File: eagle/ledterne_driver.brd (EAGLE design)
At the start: 24.3 x 23.1 mm, 10 parts, among them IC1 MEGA8-AI

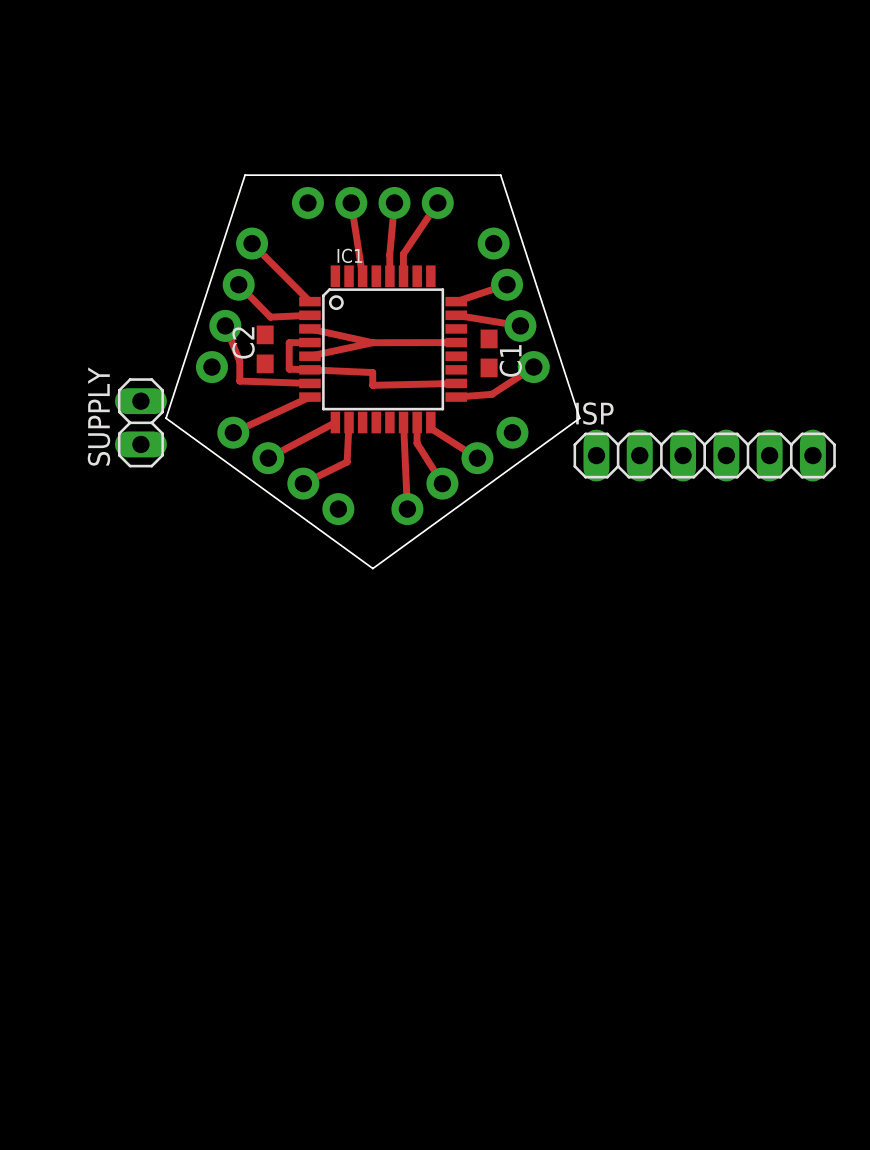
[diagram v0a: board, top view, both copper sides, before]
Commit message: Alternative routing for driver board
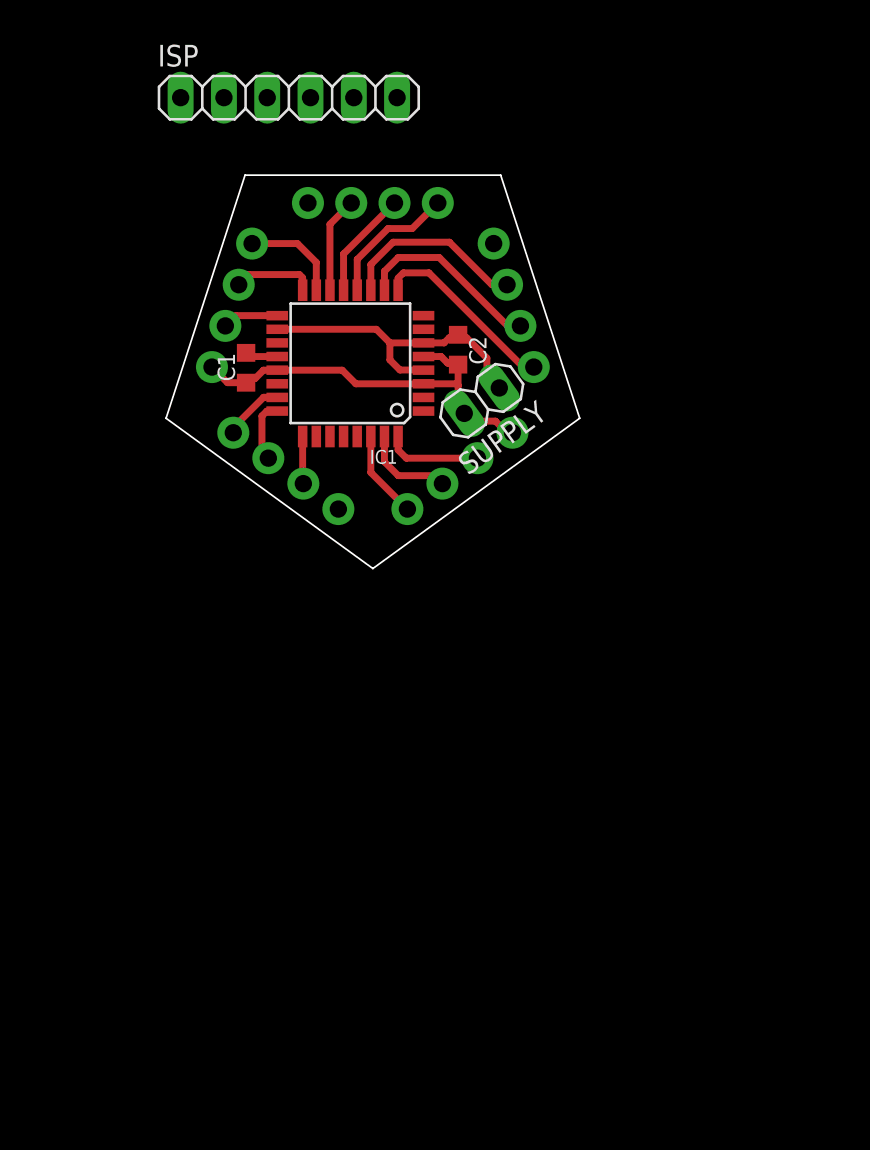
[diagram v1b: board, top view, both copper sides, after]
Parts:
- C1, C2: device rcl:C0603 -> rcl:C0603K
- moved ISP 32.2 mm to (11.6, 31.4)
- moved SUPPLY 20.0 mm to (22.9, 13.6), turned to 216 degrees
- moved C1 14.3 mm to (9.07, 15.5), turned to 90 degrees
- moved C2 11.3 mm to (21.5, 16.6), turned to 270 degrees
- moved IC1 2.09 mm to (15.2, 15.8), turned to 180 degrees
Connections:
- removed net N$2: IC1.30, JP1.3
- new net N$14: IC1.8
- new net N$15: IC1.25, JP4.3
- net MISO: now also JP5.2; no longer JP3.3
- net MOSI: now also JP5.1; no longer JP3.2
- net N$10: now also IC1.31, JP3.2; no longer IC1.10, JP4.3
- net N$11: now also IC1.32, JP3.3; no longer IC1.7, JP5.3
- net N$12: now also IC1.23; no longer IC1.8
- net N$13: now also IC1.24, JP4.2; no longer IC1.1, JP5.1
- net N$3: now also IC1.14, JP1.3; no longer IC1.28, JP1.2
- net N$4: now also IC1.13, JP1.2; no longer IC1.27, JP1.1
- net N$5: now also IC1.12, JP1.1; no longer IC1.23, JP2.2
- net N$6: now also IC1.11, JP2.3; no longer IC1.2, JP5.2
- net N$7: now also IC1.10, JP2.2; no longer IC1.24, JP2.3
- net N$8: now also IC1.9, JP2.1; no longer IC1.14, JP3.1
- net N$9: now also IC1.30, JP3.1; no longer IC1.9, JP4.2
- net SCK: now also JP5.3; no longer JP2.1
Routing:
- net GND: track 12.4 -> 24.0 mm
- net N$7: track 3.14 -> 11.1 mm
- net N$6: track 4.98 -> 11.1 mm
- net N$8: track 5.08 -> 11.1 mm
- net VCC: track 13.3 -> 18.8 mm
- net N$2: track 4.35 -> 0.00 mm
- net N$5: track 3.82 -> 7.91 mm
- net N$15: track 0.00 -> 2.78 mm
- net N$1: track 0.00 -> 1.89 mm
- net N$11: track 7.52 -> 5.64 mm
- net MOSI: track 4.01 -> 5.85 mm
- net SCK: track 5.03 -> 3.29 mm
- net N$4: track 4.91 -> 6.36 mm
- net N$12: track 4.96 -> 3.62 mm
- net N$3: track 4.31 -> 5.64 mm
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
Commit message: Replace ISP connector with solder pads
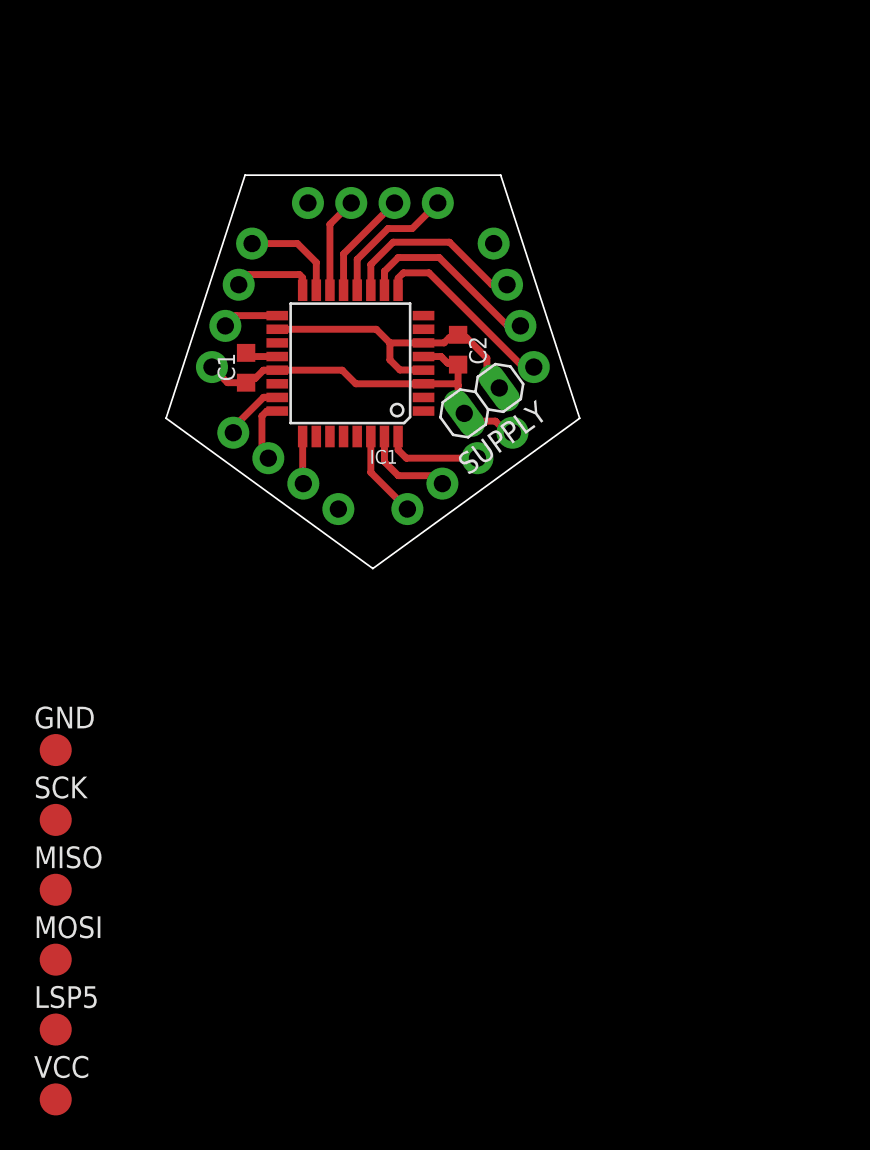
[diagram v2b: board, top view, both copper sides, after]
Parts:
- removed ISP: (no value), pinhead:1X06
- added GND, LSP5, MISO, MOSI, SCK, VCC: SOLPAD-SMD-NORMAL, solpad-smd:SOLPAD-SMD
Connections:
- net GND: now also GND.MP; no longer ISP.1
- net MISO: now also MISO.MP; no longer ISP.3
- net MOSI: now also MOSI.MP; no longer ISP.4
- net RESET: now also LSP5.MP; no longer ISP.5
- net SCK: now also SCK.MP; no longer ISP.2
- net VCC: now also VCC.MP; no longer ISP.6
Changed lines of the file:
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@@
 <attribute name="MPN" value="ATMEGA8-16AU" x="15.19" y="15.79" size="1.778" layer="27" rot="R180" display="off"/>
 </element>
-<element name="ISP" library="pinhead" package="1X06" value="" x="11.58" y="31.38"/>
 <element name="C1" library="rcl" package="C0603K" value="" x="9.07" y="15.53" rot="R90"/>
 <element name="C2" library="rcl" package="C0603K" value="" x="21.51" y="16.59" rot="R270"/>
@@
 <element name="JP5" library="pinhead_round_pads" package="1X04/90" value="" x="4.62179375" y="20.3727125" rot="MR288"/>
 <element name="SUPPLY" library="pinhead" package="1X02" value="" x="22.9" y="13.6" rot="R216"/>
+<element name="GND" library="solpad-smd" package="SOLPAD-SMD" value="SOLPAD-SMD-NORMAL" x="-2.1" y="-6.9"/>
+<element name="SCK" library="solpad-smd" package="SOLPAD-SMD" value="SOLPAD-SMD-NORMAL" x="-2.1" y="-11"/>
+<element name="MISO" library="solpad-smd" package="SOLPAD-SMD" value="SOLPAD-SMD-NORMAL" x="-2.1" y="-15.1"/>
+<element name="MOSI" library="solpad-smd" package="SOLPAD-SMD" value="SOLPAD-SMD-NORMAL" x="-2.1" y="-19.2"/>
+<element name="LSP5" library="solpad-smd" package="SOLPAD-SMD" value="SOLPAD-SMD-NORMAL" x="-2.1" y="-23.3"/>
+<element name="VCC" library="solpad-smd" package="SOLPAD-SMD" value="SOLPAD-SMD-NORMAL" x="-2.1" y="-27.4"/>
 </elements>
 <signals>
 <signal name="GND">
-<contactref element="ISP" pad="1"/>
 <contactref element="IC1" pad="21"/>
 <contactref element="IC1" pad="3"/>
@@
 <wire x1="23.7" y1="12.4" x2="24.380896875" y2="11.719103125" width="0.4064" layer="1"/>
 <wire x1="24.380896875" y1="11.719103125" x2="24.700209375" y2="11.719103125" width="0.4064" layer="1"/>
-<wire x1="20.51" y1="16.19" x2="23.597328125" y2="22.81888125" width="0" layer="19" extent="1-1"/>
-<wire x1="14.484503125" y1="7.240178125" x2="15.51" y2="14.59" width="0" layer="19" extent="1-1"/>
-<wire x1="12.7" y1="25.2" x2="10.8974" y2="15.39" width="0" layer="19" extent="1-1"/>
-<wire x1="5.23" y1="31.38" x2="12.7" y2="25.2" width="0" layer="19" extent="1-1"/>
 <wire x1="10.8974" y1="15.39" x2="10.09" y2="15.39" width="0.4064" layer="1"/>
 <wire x1="10.09" y1="15.39" x2="9.6" y2="14.9" width="0.4064" layer="1"/>
 <wire x1="9.6" y1="14.9" x2="9.315" y2="14.9" width="0.4064" layer="1"/>
 <wire x1="9.315" y1="14.9" x2="9.07" y2="14.655" width="0.4064" layer="1"/>
+<contactref element="GND" pad="MP"/>
+<wire x1="20.51" y1="16.19" x2="23.597328125" y2="22.81888125" width="0" layer="19" extent="1-1"/>
+<wire x1="14.484503125" y1="7.240178125" x2="15.51" y2="14.59" width="0" layer="19" extent="1-1"/>
+<wire x1="12.7" y1="25.2" x2="10.8974" y2="15.39" width="0" layer="19" extent="1-1"/>
+<wire x1="-2.1" y1="-6.9" x2="14.484503125" y2="7.240178125" width="0" layer="19" extent="1-1"/>
 </signal>
 <signal name="VCC">
-<contactref element="ISP" pad="6"/>
 <contactref element="IC1" pad="4"/>
 <contactref element="IC1" pad="6"/>
@@
 <wire x1="23.2" y1="16.1" x2="23.2" y2="15.073934375" width="0.4064" layer="1"/>
 <wire x1="23.2" y1="15.073934375" x2="23.92745" y2="14.346484375" width="0.4064" layer="1"/>
-<wire x1="16.71" y1="17.79" x2="17.93" y2="31.38" width="0" layer="19" extent="1-1"/>
+<contactref element="VCC" pad="MP"/>
+<wire x1="-2.1" y1="-27.4" x2="10.8974" y2="17.79" width="0" layer="19" extent="1-1"/>
 </signal>
 <signal name="RESET">
 <contactref element="IC1" pad="29"/>
-<contactref element="ISP" pad="5"/>
-<wire x1="15.59" y1="11.4974" x2="15.39" y2="31.38" width="0" layer="19" extent="1-1"/>
+<contactref element="LSP5" pad="MP"/>
+<wire x1="-2.1" y1="-23.3" x2="15.59" y2="11.4974" width="0" layer="19" extent="1-1"/>
 </signal>
 <signal name="MOSI">
 <contactref element="IC1" pad="15"/>
-<contactref element="ISP" pad="4"/>
 <contactref element="JP5" pad="1"/>
 <wire x1="9.422671875" y1="22.81888125" x2="12.08111875" y2="22.81888125" width="0.4064" layer="1"/>
 <wire x1="12.08111875" y1="22.81888125" x2="13.19" y2="21.71" width="0.4064" layer="1"/>
 <wire x1="13.19" y1="21.71" x2="13.19" y2="20.0826" width="0.4064" layer="1"/>
-<wire x1="12.08111875" y1="22.81888125" x2="12.85" y2="31.38" width="0" layer="19" extent="1-1"/>
+<contactref element="MOSI" pad="MP"/>
+<wire x1="-2.1" y1="-19.2" x2="13.19" y2="20.0826" width="0" layer="19" extent="1-1"/>
 </signal>
 <signal name="MISO">
 <contactref element="IC1" pad="16"/>
-<contactref element="ISP" pad="3"/>
 <contactref element="JP5" pad="2"/>
 <wire x1="12.39" y1="20.0826" x2="12.39" y2="20.81" width="0.4064" layer="1"/>
@@
 <wire x1="12.2" y1="21" x2="9.234575" y2="21" width="0.4064" layer="1"/>
 <wire x1="9.234575" y1="21" x2="8.637771875" y2="20.403196875" width="0.4064" layer="1"/>
-<wire x1="9.234575" y1="21" x2="10.31" y2="31.38" width="0" layer="19" extent="1-1"/>
+<contactref element="MISO" pad="MP"/>
+<wire x1="-2.1" y1="-15.1" x2="8.637771875" y2="20.403196875" width="0" layer="19" extent="1-1"/>
 </signal>
 <signal name="SCK">
 <contactref element="IC1" pad="17"/>
-<contactref element="ISP" pad="2"/>
 <contactref element="JP5" pad="3"/>
 <wire x1="7.85286875" y1="17.987515625" x2="8.455353125" y2="18.59" width="0.4064" layer="1"/>
 <wire x1="8.455353125" y1="18.59" x2="10.8974" y2="18.59" width="0.4064" layer="1"/>
-<wire x1="8.455353125" y1="18.59" x2="7.77" y2="31.38" width="0" layer="19" extent="1-1"/>
+<contactref element="SCK" pad="MP"/>
+<wire x1="-2.1" y1="-11" x2="7.85286875" y2="17.987515625" width="0" layer="19" extent="1-1"/>
 </signal>
 <signal name="N$1">

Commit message: Place ISP solder pads on the board
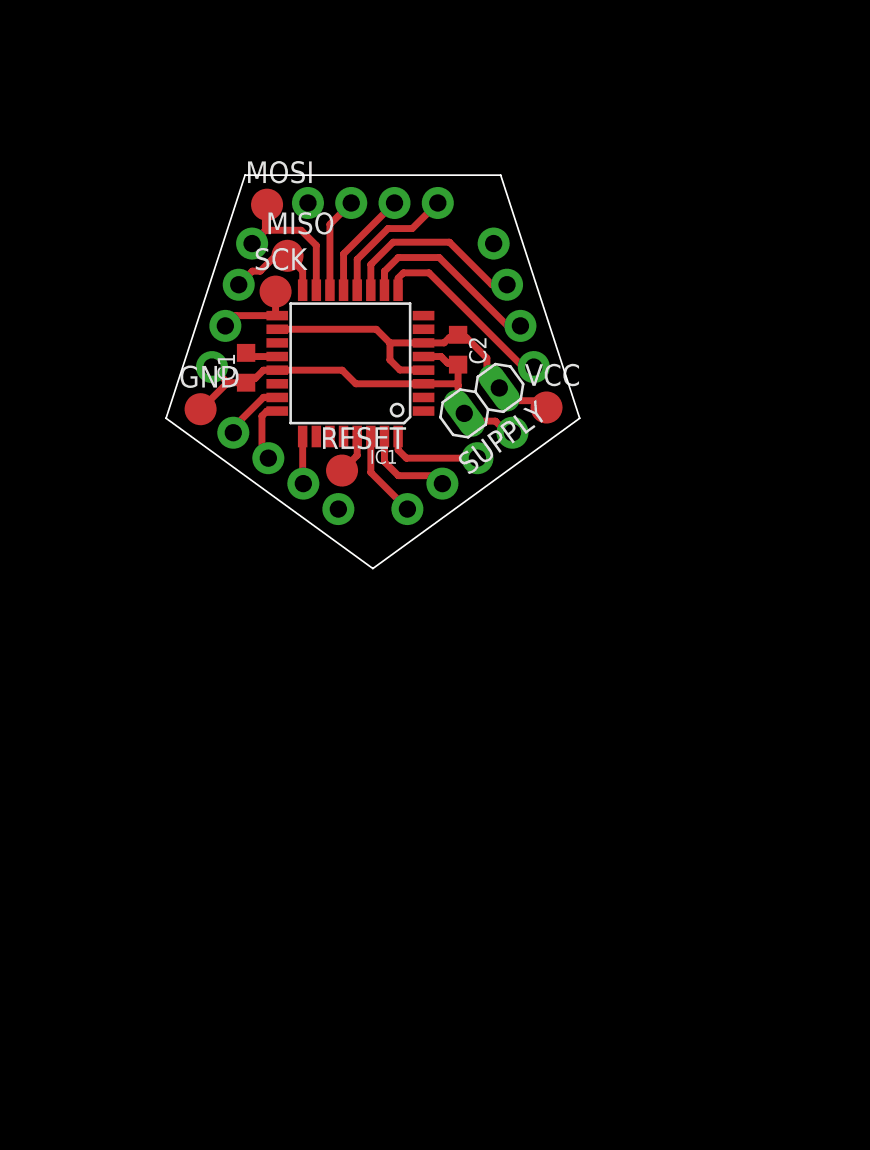
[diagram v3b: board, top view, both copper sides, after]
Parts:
- removed LSP5: SOLPAD-SMD-NORMAL, solpad-smd:SOLPAD-SMD
- added RESET: SOLPAD-SMD-NORMAL, solpad-smd:SOLPAD-SMD
- moved VCC 49.8 mm to (26.7, 13.2)
- moved MOSI 46.0 mm to (10.3, 25.1)
- moved MISO 39.6 mm to (11.5, 22.1)
- moved SCK 33.6 mm to (10.8, 20.0)
- moved GND 21.7 mm to (6.40, 13.1)
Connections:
- net RESET: now also RESET.MP; no longer LSP5.MP
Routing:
- net VCC: track 18.8 -> 22.0 mm
- net MOSI: track 5.85 -> 8.63 mm
- net RESET: track 0.00 -> 2.37 mm
- net GND: track 24.0 -> 26.3 mm
- net SCK: track 3.29 -> 4.80 mm
- net MISO: track 4.81 -> 5.95 mm
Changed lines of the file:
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@@
 <element name="JP5" library="pinhead_round_pads" package="1X04/90" value="" x="4.62179375" y="20.3727125" rot="MR288"/>
 <element name="SUPPLY" library="pinhead" package="1X02" value="" x="22.9" y="13.6" rot="R216"/>
-<element name="GND" library="solpad-smd" package="SOLPAD-SMD" value="SOLPAD-SMD-NORMAL" x="-2.1" y="-6.9"/>
-<element name="SCK" library="solpad-smd" package="SOLPAD-SMD" value="SOLPAD-SMD-NORMAL" x="-2.1" y="-11"/>
-<element name="MISO" library="solpad-smd" package="SOLPAD-SMD" value="SOLPAD-SMD-NORMAL" x="-2.1" y="-15.1"/>
-<element name="MOSI" library="solpad-smd" package="SOLPAD-SMD" value="SOLPAD-SMD-NORMAL" x="-2.1" y="-19.2"/>
-<element name="LSP5" library="solpad-smd" package="SOLPAD-SMD" value="SOLPAD-SMD-NORMAL" x="-2.1" y="-23.3"/>
-<element name="VCC" library="solpad-smd" package="SOLPAD-SMD" value="SOLPAD-SMD-NORMAL" x="-2.1" y="-27.4"/>
+<element name="GND" library="solpad-smd" package="SOLPAD-SMD" value="SOLPAD-SMD-NORMAL" x="6.4" y="13.1"/>
+<element name="SCK" library="solpad-smd" package="SOLPAD-SMD" value="SOLPAD-SMD-NORMAL" x="10.8" y="20"/>
+<element name="MISO" library="solpad-smd" package="SOLPAD-SMD" value="SOLPAD-SMD-NORMAL" x="11.5" y="22.1"/>
+<element name="MOSI" library="solpad-smd" package="SOLPAD-SMD" value="SOLPAD-SMD-NORMAL" x="10.3" y="25.1"/>
+<element name="RESET" library="solpad-smd" package="SOLPAD-SMD" value="SOLPAD-SMD-NORMAL" x="14.7" y="9.5"/>
+<element name="VCC" library="solpad-smd" package="SOLPAD-SMD" value="SOLPAD-SMD-NORMAL" x="26.7" y="13.2"/>
 </elements>
 <signals>
@@
 <wire x1="9.315" y1="14.9" x2="9.07" y2="14.655" width="0.4064" layer="1"/>
 <contactref element="GND" pad="MP"/>
+<wire x1="6.4" y1="13.1" x2="6.429796875" y2="13.1" width="0.4064" layer="1"/>
+<wire x1="6.429796875" y1="13.1" x2="7.984796875" y2="14.655" width="0.4064" layer="1"/>
 <wire x1="20.51" y1="16.19" x2="23.597328125" y2="22.81888125" width="0" layer="19" extent="1-1"/>
 <wire x1="14.484503125" y1="7.240178125" x2="15.51" y2="14.59" width="0" layer="19" extent="1-1"/>
 <wire x1="12.7" y1="25.2" x2="10.8974" y2="15.39" width="0" layer="19" extent="1-1"/>
-<wire x1="-2.1" y1="-6.9" x2="14.484503125" y2="7.240178125" width="0" layer="19" extent="1-1"/>
 </signal>
 <signal name="VCC">
@@
 <wire x1="23.2" y1="15.073934375" x2="23.92745" y2="14.346484375" width="0.4064" layer="1"/>
 <contactref element="VCC" pad="MP"/>
-<wire x1="-2.1" y1="-27.4" x2="10.8974" y2="17.79" width="0" layer="19" extent="1-1"/>
+<wire x1="24.673934375" y1="13.6" x2="26.3" y2="13.6" width="0.4064" layer="1"/>
+<wire x1="26.3" y1="13.6" x2="26.7" y2="13.2" width="0.4064" layer="1"/>
+<wire x1="24.673934375" y1="13.6" x2="23.92745" y2="14.346484375" width="0.4064" layer="1"/>
 </signal>
 <signal name="RESET">
 <contactref element="IC1" pad="29"/>
-<contactref element="LSP5" pad="MP"/>
-<wire x1="-2.1" y1="-23.3" x2="15.59" y2="11.4974" width="0" layer="19" extent="1-1"/>
+<contactref element="RESET" pad="MP"/>
+<wire x1="15.59" y1="11.4974" x2="15.59" y2="10.39" width="0.4064" layer="1"/>
+<wire x1="15.59" y1="10.39" x2="14.7" y2="9.5" width="0.4064" layer="1"/>
 </signal>
 <signal name="MOSI">
 <contactref element="IC1" pad="15"/>
 <contactref element="JP5" pad="1"/>
-<wire x1="9.422671875" y1="22.81888125" x2="12.08111875" y2="22.81888125" width="0.4064" layer="1"/>
-<wire x1="12.08111875" y1="22.81888125" x2="13.19" y2="21.71" width="0.4064" layer="1"/>
-<wire x1="13.19" y1="21.71" x2="13.19" y2="20.0826" width="0.4064" layer="1"/>
+<wire x1="13.19" y1="22.71" x2="13.19" y2="20.0826" width="0.4064" layer="1"/>
 <contactref element="MOSI" pad="MP"/>
-<wire x1="-2.1" y1="-19.2" x2="13.19" y2="20.0826" width="0" layer="19" extent="1-1"/>
+<wire x1="13.19" y1="22.71" x2="12.3" y2="23.6" width="0.4064" layer="1"/>
+<wire x1="12.3" y1="23.6" x2="10.203790625" y2="23.6" width="0.4064" layer="1"/>
+<wire x1="10.203790625" y1="23.6" x2="9.422671875" y2="22.81888125" width="0.4064" layer="1"/>
+<wire x1="10.203790625" y1="23.6" x2="10.203790625" y2="25.003790625" width="0.4064" layer="1"/>
+<wire x1="10.203790625" y1="25.003790625" x2="10.3" y2="25.1" width="0.4064" layer="1"/>
 </signal>
 <signal name="MISO">
 <contactref element="IC1" pad="16"/>
 <contactref element="JP5" pad="2"/>
-<wire x1="12.39" y1="20.0826" x2="12.39" y2="20.81" width="0.4064" layer="1"/>
-<wire x1="12.39" y1="20.81" x2="12.2" y2="21" width="0.4064" layer="1"/>
-<wire x1="12.2" y1="21" x2="9.234575" y2="21" width="0.4064" layer="1"/>
-<wire x1="9.234575" y1="21" x2="8.637771875" y2="20.403196875" width="0.4064" layer="1"/>
 <contactref element="MISO" pad="MP"/>
-<wire x1="-2.1" y1="-15.1" x2="8.637771875" y2="20.403196875" width="0" layer="19" extent="1-1"/>
+<wire x1="12.39" y1="20.0826" x2="12.39" y2="21.21" width="0.4064" layer="1"/>
+<wire x1="12.39" y1="21.21" x2="11.5" y2="22.1" width="0.4064" layer="1"/>
+<wire x1="11.5" y1="22.1" x2="10.8" y2="22.1" width="0.4064" layer="1"/>
+<wire x1="10.8" y1="22.1" x2="9.9" y2="21.2" width="0.4064" layer="1"/>
+<wire x1="9.9" y1="21.2" x2="9.434575" y2="21.2" width="0.4064" layer="1"/>
+<wire x1="9.434575" y1="21.2" x2="8.637771875" y2="20.403196875" width="0.4064" layer="1"/>
 </signal>
 <signal name="SCK">
@@
 <wire x1="8.455353125" y1="18.59" x2="10.8974" y2="18.59" width="0.4064" layer="1"/>
 <contactref element="SCK" pad="MP"/>
-<wire x1="-2.1" y1="-11" x2="7.85286875" y2="17.987515625" width="0" layer="19" extent="1-1"/>
+<wire x1="10.8974" y1="18.59" x2="10.8" y2="18.59" width="0.4064" layer="1"/>
+<wire x1="10.8" y1="18.59" x2="10.8" y2="20" width="0.4064" layer="1"/>
 </signal>
 <signal name="N$1">
